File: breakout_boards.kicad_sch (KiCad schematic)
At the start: 10 parts, among them J1 Conn_01x04, J2 Conn_01x04

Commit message: first draft
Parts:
- added J3, J4: Conn_01x04, Connector_PinHeader_2.54mm:PinHeader_1x04_P2.54mm_Vertical, symbol Connector_Generic:Conn_01x04
- added SW1: RotaryEncoder, symbol Device:RotaryEncoder
- added SW2: RotaryEncoder_Switch, symbol Device:RotaryEncoder_Switch
- added SW3: SW_SPST, symbol Switch:SW_SPST

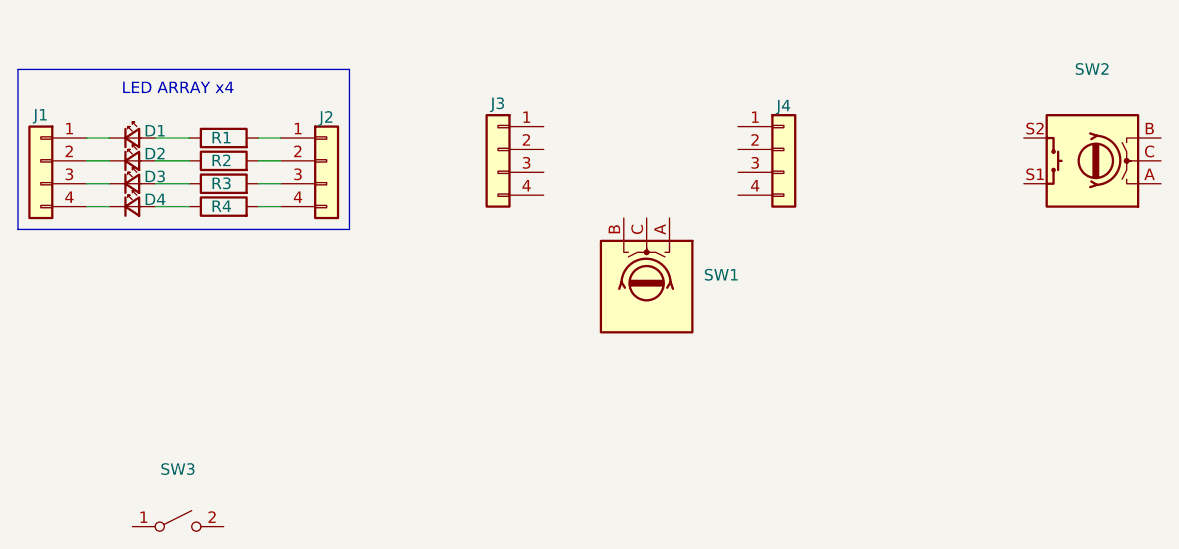
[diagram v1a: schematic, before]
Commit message: updated gitignore and added single keyboard switch, with debouncing
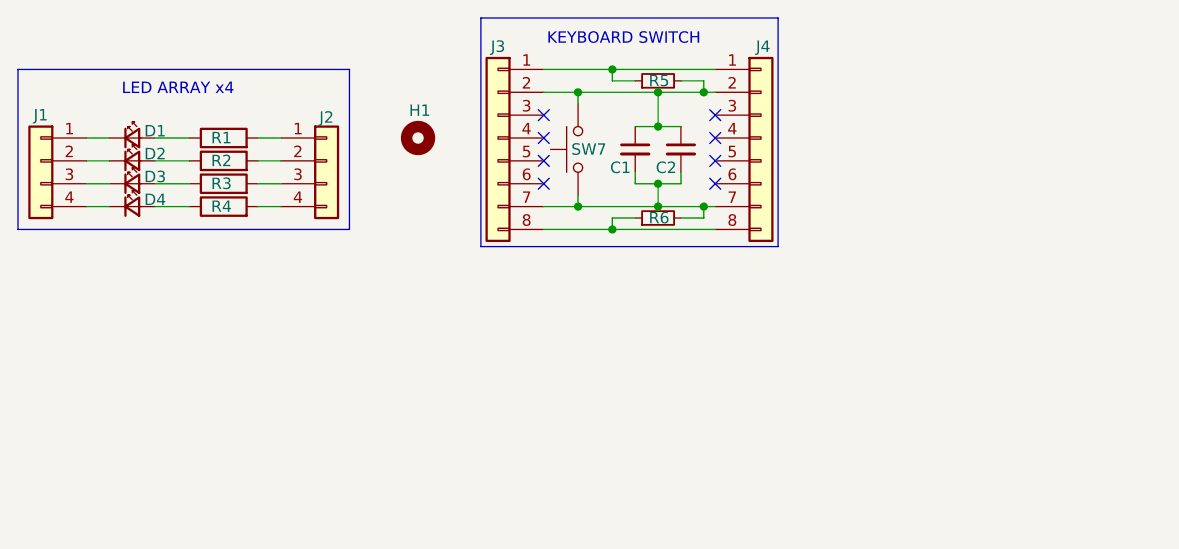
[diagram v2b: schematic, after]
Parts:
- removed J3, J4: Conn_01x04, Connector_PinHeader_2.54mm:PinHeader_1x04_P2.54mm_Vertical, symbol Connector_Generic:Conn_01x04
- removed SW1: RotaryEncoder, symbol Device:RotaryEncoder
- removed SW2: RotaryEncoder_Switch, symbol Device:RotaryEncoder_Switch
- removed SW3: SW_SPST, symbol Switch:SW_SPST
- added C1, C2: C_Small, Capacitor_SMD:C_1206_3216Metric_Pad1.33x1.80mm_HandSolder, symbol Device:C_Small
- added H1: MountingHole, Panelization:mouse-bite-2.54mm-slot, symbol Mechanical:MountingHole
- added J3, J4: Conn_01x08, Connector_PinHeader_2.54mm:PinHeader_1x08_P2.54mm_Vertical, symbol Connector_Generic:Conn_01x08
- added R5, R6: R_Small, Resistor_SMD:R_1206_3216Metric_Pad1.30x1.75mm_HandSolder, symbol Device:R_Small
- added SW7: SW_Push, Button_Switch_Keyboard:SW_Hotswap_Kailh_MX_1.00u, symbol Switch:SW_Push
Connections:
- new net: J3.1 (Pin_1), J4.1 (Pin_1), R5.1
- new net: C1.1, C2.1, J3.2 (Pin_2), J4.2 (Pin_2), R5.2, SW7.2
- new net: C1.2, C2.2, J3.7 (Pin_7), J4.7 (Pin_7), R6.2, SW7.1
- new net: J3.8 (Pin_8), J4.8 (Pin_8), R6.1
- no-connect marks 0 -> 8
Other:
- note added: "KEYBOARD SWITCH"

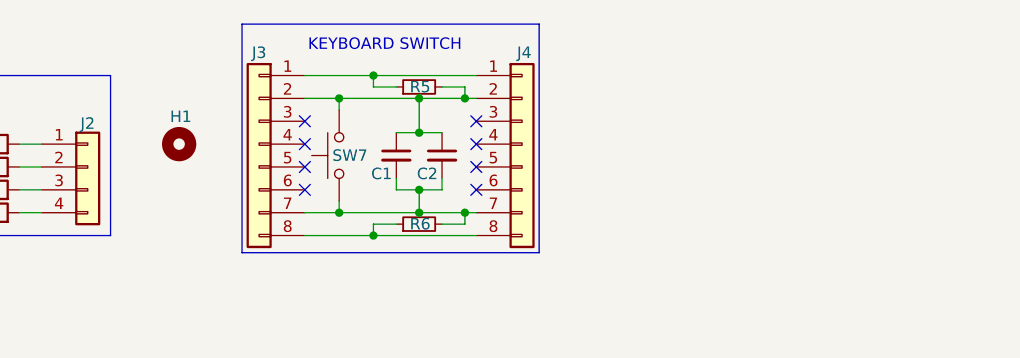
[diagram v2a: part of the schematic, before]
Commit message: added matrix keyboard pending to remove unused pins and use more header pins
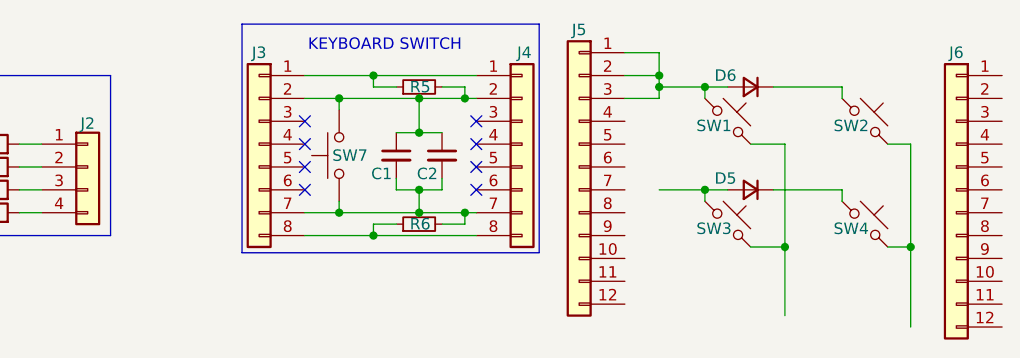
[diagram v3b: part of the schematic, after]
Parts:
- removed H1: MountingHole, Panelization:mouse-bite-2.54mm-slot, symbol Mechanical:MountingHole
- added D5, D6: D_Small, Diode_SMD:D_1206_3216Metric_Pad1.42x1.75mm_HandSolder, symbol Device:D_Small
- added J5, J6: Conn_01x12, Connector_PinHeader_2.54mm:PinHeader_1x12_P2.54mm_Vertical, symbol Connector_Generic:Conn_01x12
- added SW1, SW2, SW3, SW4: SW_Push_45deg, Button_Switch_THT:SW_PUSH-12mm, symbol Switch:SW_Push_45deg
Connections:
- new net: D5.1 (K), SW4.1
- new net: SW2.2, SW4.2
- new net: D5.2 (A), SW3.1
- new net: D6.1 (K), SW2.1
- new net: D6.2 (A), J5.1 (Pin_1), J5.2 (Pin_2), J5.3 (Pin_3), SW1.1
- new net: SW1.2, SW3.2

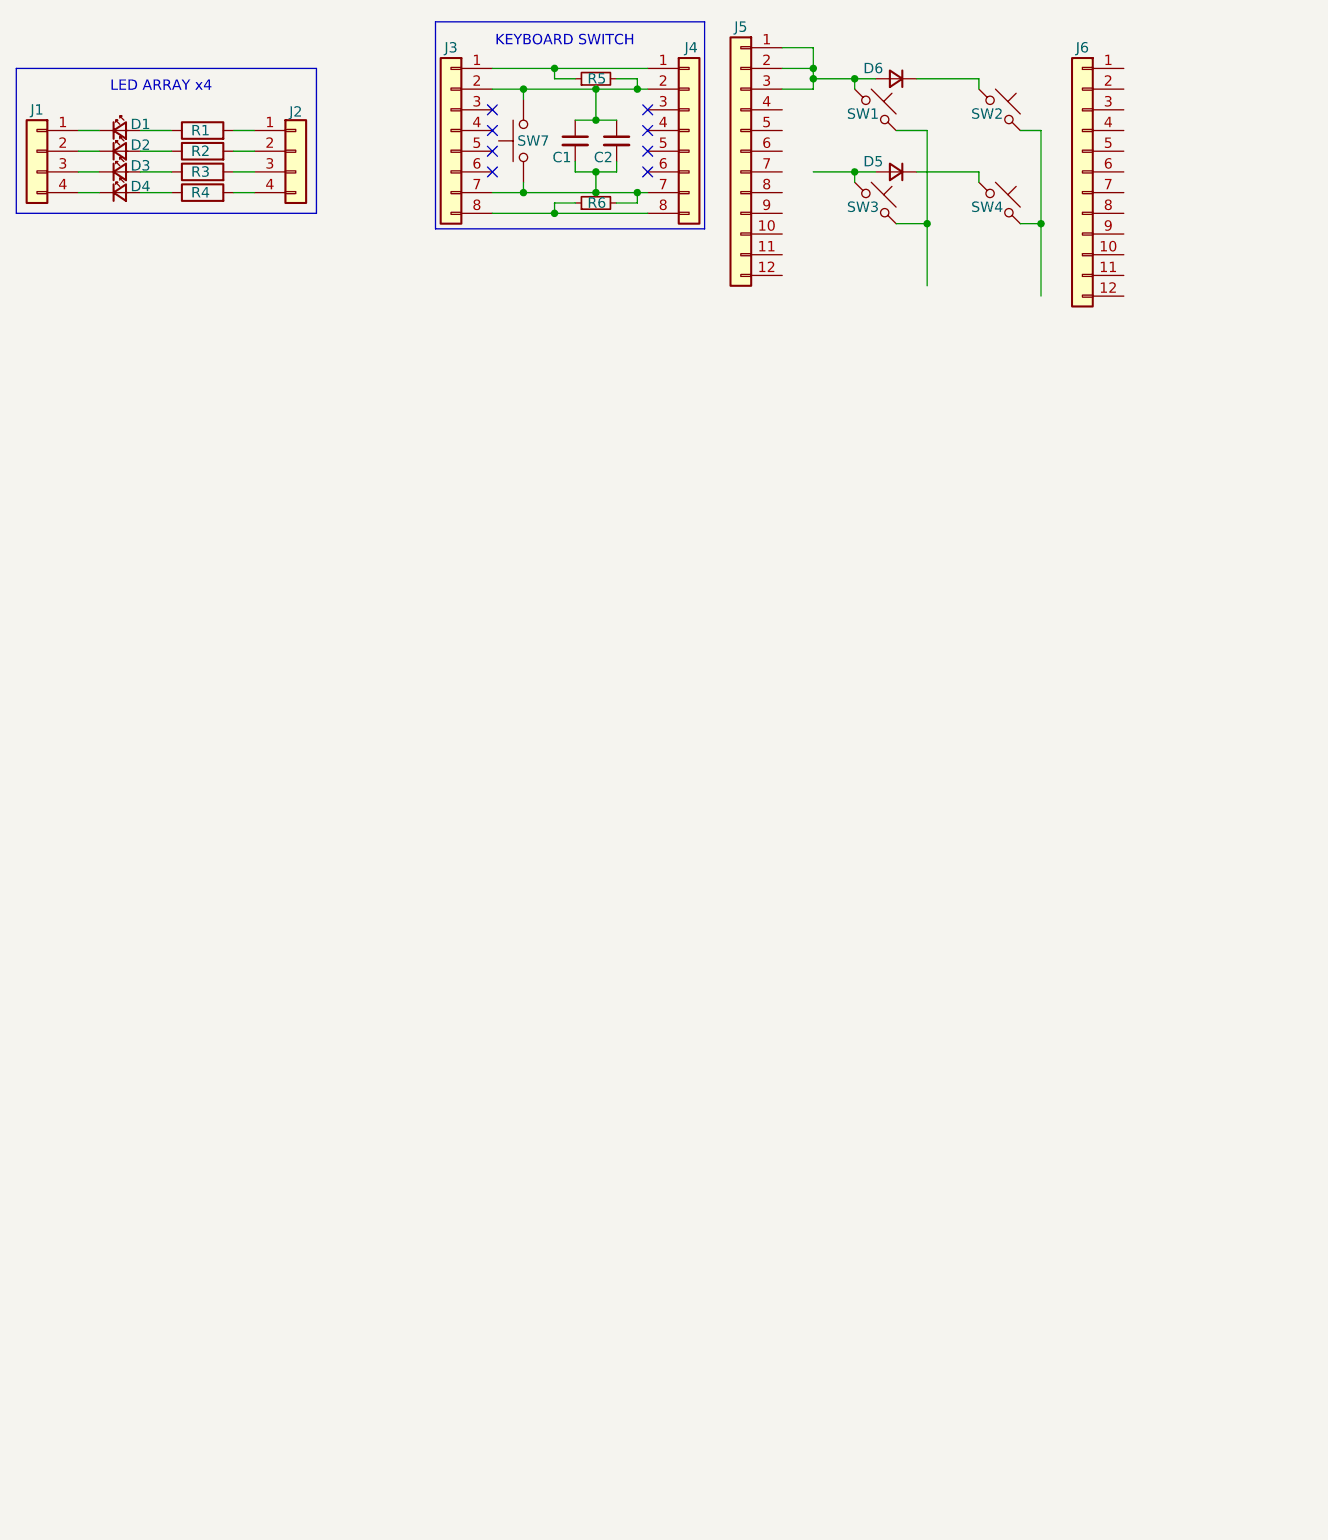
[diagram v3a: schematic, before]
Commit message: refactored pcb, added led matrix
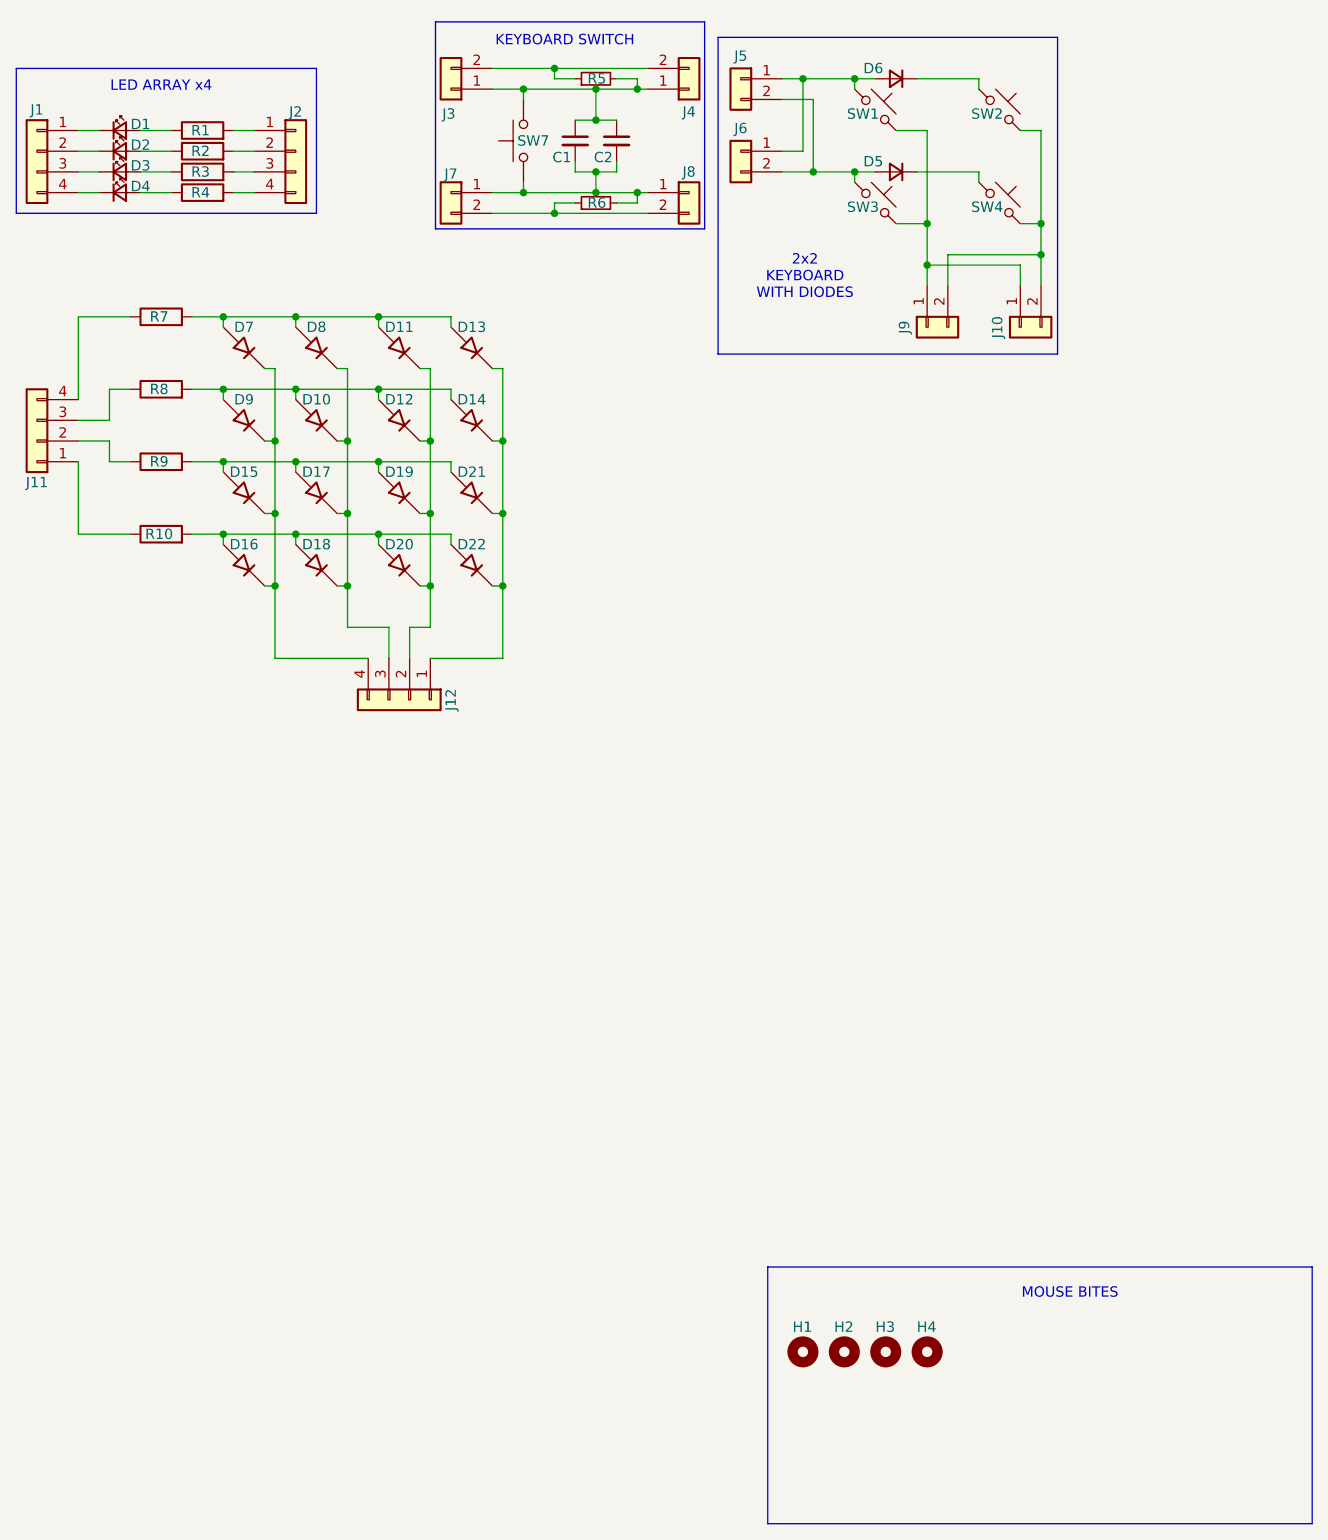
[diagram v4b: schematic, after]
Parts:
- removed J3, J4: Conn_01x08, Connector_PinHeader_2.54mm:PinHeader_1x08_P2.54mm_Vertical, symbol Connector_Generic:Conn_01x08
- removed J5, J6: Conn_01x12, Connector_PinHeader_2.54mm:PinHeader_1x12_P2.54mm_Vertical, symbol Connector_Generic:Conn_01x12
- added D10, D11, D12, D13, D14, D15, D16, D17, D18, D19, D20, D21, D22, D7, D8, D9: D_45deg, LED_SMD:LED_1206_3216Metric_Pad1.42x1.75mm_HandSolder, symbol Device:D_45deg
- added H1, H2, H3, H4: MountingHole, Panelization:mouse-bite-2.54mm-slot, symbol Mechanical:MountingHole
- added J10, J3, J4, J5, J6, J7, J8, J9: Conn_01x02, Connector_PinHeader_2.54mm:PinHeader_1x02_P2.54mm_Vertical, symbol Connector_Generic:Conn_01x02
- added J11, J12: Conn_01x04, Connector_PinHeader_2.54mm:PinHeader_1x04_P2.54mm_Vertical, symbol Connector_Generic:Conn_01x04
- added R10, R7, R8, R9: R, Resistor_SMD:R_1206_3216Metric_Pad1.30x1.75mm_HandSolder, symbol Device:R
- D5, D6: footprint Diode_SMD:D_1206_3216Metric_Pad1.42x1.75mm_HandSolder -> Diode_THT:D_DO-35_SOD27_P7.62mm_Horizontal
- SW1, SW2, SW3, SW4: footprint Button_Switch_THT:SW_PUSH-12mm -> Button_Switch_THT:SW_PUSH_6mm
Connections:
- net at R5.1: now also J3.2 (Pin_2), J4.2 (Pin_2)
- net at C1.1, C2.1, R5.2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: now also J3.1 (Pin_1), J4.1 (Pin_1)
- net at C1.2, C2.2, R6.2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: now also J7.1 (Pin_1), J8.1 (Pin_1)
- net at R6.1: now also J7.2 (Pin_2), J8.2 (Pin_2)
- net at SW2.2, SW4.2: now also J10.2 (Pin_2), J9.2 (Pin_2)
- net at D5.2 (A), SW3.1: now also J5.2 (Pin_2), J6.2 (Pin_2)
- net at D6.2 (A), SW1.1: now also J5.1 (Pin_1), J6.1 (Pin_1)
- net at SW1.2, SW3.2: now also J10.1 (Pin_1), J9.1 (Pin_1)
- new net: D10.1 (K), D17.1 (K), D18.1 (K), D8.1 (K), J12.3 (Pin_3)
- new net: D10.2 (A), D12.2 (A), D14.2 (A), D9.2 (A), R8.2
- new net: D15.1 (K), D16.1 (K), D7.1 (K), D9.1 (K), J12.4 (Pin_4)
- new net: J11.1 (Pin_1), R10.1
- new net: D16.2 (A), D18.2 (A), D20.2 (A), D22.2 (A), R10.2
- new net: D13.1 (K), D14.1 (K), D21.1 (K), D22.1 (K), J12.1 (Pin_1)
- new net: D11.2 (A), D13.2 (A), D7.2 (A), D8.2 (A), R7.2
- new net: J11.2 (Pin_2), R9.1
- new net: D15.2 (A), D17.2 (A), D19.2 (A), D21.2 (A), R9.2
- new net: J11.3 (Pin_3), R8.1
- new net: D11.1 (K), D12.1 (K), D19.1 (K), D20.1 (K), J12.2 (Pin_2)
- new net: J11.4 (Pin_4), R7.1
- no-connect marks 8 -> 0
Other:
- note added: "2x2 KEYBOARD WITH DIODES"
- note added: "MOUSE BITES"

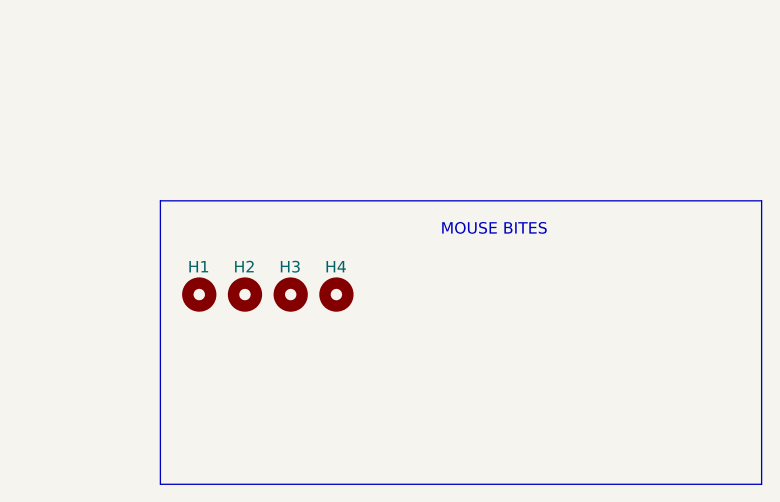
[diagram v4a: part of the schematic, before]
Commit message: added missing mounting holes
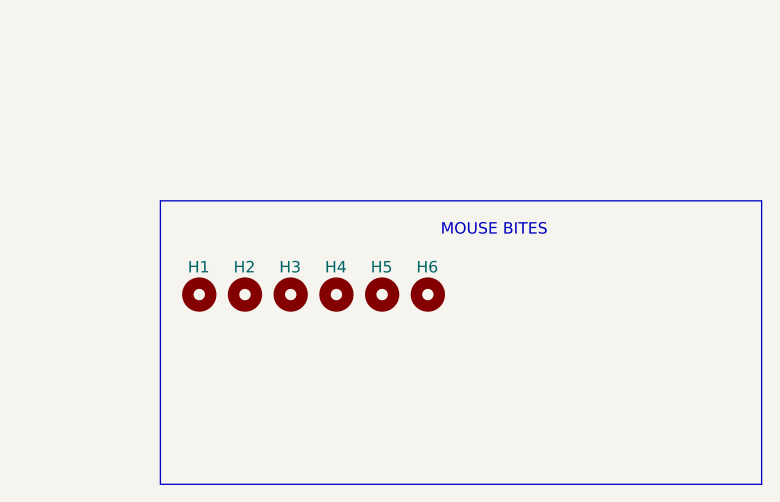
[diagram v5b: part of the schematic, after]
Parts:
- added H5, H6: MountingHole, Panelization:mouse-bite-2.54mm-slot, symbol Mechanical:MountingHole
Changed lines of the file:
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@@
+	)
+	(symbol
+		(lib_id "Mechanical:MountingHole")
+		(at 139.7 176.53 0)
+		(unit 1)
+		(exclude_from_sim yes)
+		(in_bom no)
+		(on_board yes)
+		(dnp no)
+		(property "Reference" "H6"
+			(at 138.43 173.482 0)
+			(effects
+				(font
+					(size 1.27 1.27)
+				)
+				(justify left)
+			)
+		)
+		(property "Value" "MountingHole"
+			(at 142.24 177.7999 0)
+			(effects
+				(font
+					(size 1.27 1.27)
+				)
+				(justify left)
+				(hide yes)
+			)
+		)
+		(property "Footprint" "Panelization:mouse-bite-2.54mm-slot"
+			(at 139.7 176.53 0)
+			(effects
+				(font
+					(size 1.27 1.27)
+				)
+				(hide yes)
+			)
+		)
+		(property "Datasheet" "~"
+			(at 139.7 176.53 0)
+			(effects
+				(font
+					(size 1.27 1.27)
+				)
+				(hide yes)
+			)
+		)
+		(property "Description" "Mounting Hole without connection"
+			(at 139.7 176.53 0)
+			(effects
+				(font
+					(size 1.27 1.27)
+				)
+				(hide yes)
+			)
+		)
+		(instances
+			(project "breakout_boards"
+				(path "/58919bbd-a00c-49c9-99a2-ac9ecba46a15"
+					(reference "H6")
+					(unit 1)
+				)
+			)
+		)
 	)
 	(symbol
@@
 					(unit 1)
 				)
+			)
+		)
+	)
+	(symbol
+		(lib_id "Mechanical:MountingHole")
+		(at 134.62 176.53 0)
+		(unit 1)
+		(exclude_from_sim yes)
+		(in_bom no)
+		(on_board yes)
+		(dnp no)
+		(property "Reference" "H5"
+			(at 133.35 173.482 0)
+			(effects
+				(font
+					(size 1.27 1.27)
+				)
+				(justify left)
+			)
+		)
+		(property "Value" "MountingHole"
+			(at 137.16 177.7999 0)
+			(effects
+				(font
+					(size 1.27 1.27)
+				)
+				(justify left)
+				(hide yes)
+			)
+		)
+		(property "Footprint" "Panelization:mouse-bite-2.54mm-slot"
+			(at 134.62 176.53 0)
+			(effects
+				(font
+					(size 1.27 1.27)
+				)
+				(hide yes)
+			)
+		)
+		(property "Datasheet" "~"
+			(at 134.62 176.53 0)
+			(effects
+				(font
+					(size 1.27 1.27)
+				)
+				(hide yes)
+			)
+		)
+		(property "Description" "Mounting Hole without connection"
+			(at 134.62 176.53 0)
+			(effects
+				(font
+					(size 1.27 1.27)
+				)
+				(hide yes)
+			)
+		)
+		(instances
+			(project "breakout_boards"
+				(path "/58919bbd-a00c-49c9-99a2-ac9ecba46a15"
+					(reference "H5")
+					(unit 1)
+				)
